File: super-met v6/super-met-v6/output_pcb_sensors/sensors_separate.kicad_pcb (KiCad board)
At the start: 2 copper layers, 99.3 x 99.3 mm, 66 parts, among them J4 Conn_01x08, J5 Conn_01x08, J6 Conn_01x08, J7 Conn_01x04, J8 Conn_01x04, Q13 AO3400A, Q14 AO3400A, Q15 AO3400A, Q16 AO3400A, Q17 AO3400A, Q18 AO3400A, Q19 AO3400A, Q20 AO3400A, Q21 AO3400A, Q22 AO3400A, Q23 AO3400A, Q24 AO3400A, U15 MQ GENERIC BOARD SENSOR, U16 MQ GENERIC BOARD SENSOR, U17 MQ GENERIC BOARD SENSOR, U18 MQ GENERIC BOARD SENSOR, U19 MQ GENERIC BOARD SENSOR, U20 MQ GENERIC BOARD SENSOR, U21 MQ GENERIC BOARD SENSOR, U22 MQ GENERIC BOARD SENSOR, U23 AHT10 MODULE, U24 MQ GENERIC BOARD SENSOR, U25 MQ GENERIC BOARD SENSOR, U26 MICS-6814, U27 CCS811, U28 MS-1100

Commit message: before fill
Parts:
- moved R15 79.3 mm to (67.8, 87.1)
- moved R28 79.3 mm to (83.8, 105.3)
- moved REF**20 79.3 mm to (57.7, 102.4)
- moved REF**22 79.3 mm to (88.3, 75.1)
- moved U23 79.3 mm to (108.0, 107.0)
- moved U27 79.3 mm to (102.7, 90.0)
- moved J4 79.3 mm to (30.8, 33.7)
- moved J5 79.3 mm to (30.8, 65.4)
- moved J6 79.3 mm to (30.8, 96.8)
- moved J7 79.3 mm to (113.6, 91.2)
- moved Q13 79.3 mm to (43.1, 50.9)
- moved Q15 79.3 mm to (84.3, 50.9)
- moved Q16 79.3 mm to (105.2, 51.1)
- moved Q17 79.3 mm to (43.1, 84.8)
- moved Q19 79.3 mm to (84.9, 84.1)
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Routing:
- net Board_0-/Sensors/s1_out: track 28.9 -> 24.9 mm

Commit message: filled
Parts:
- added ?: , , F.Cu at (26.5, 22.3)
- added ?: , , F.Cu at (74.7, 60.9)
- added H2: MountingHole, MountingHole:MountingHole_3.2mm_M3, F.Cu at (108.8, 109.9)
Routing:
- net Board_0-GND2: track 379.3 -> 382.5 mm
- net Board_0-/Sensors/5.2v: track 354.4 -> 353.8 mm
- added copper zone on B.Cu, net (none)
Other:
- board text added: "mq&sensors board"
- board text added: "super-met v0.1"
- board text added: "v&v"

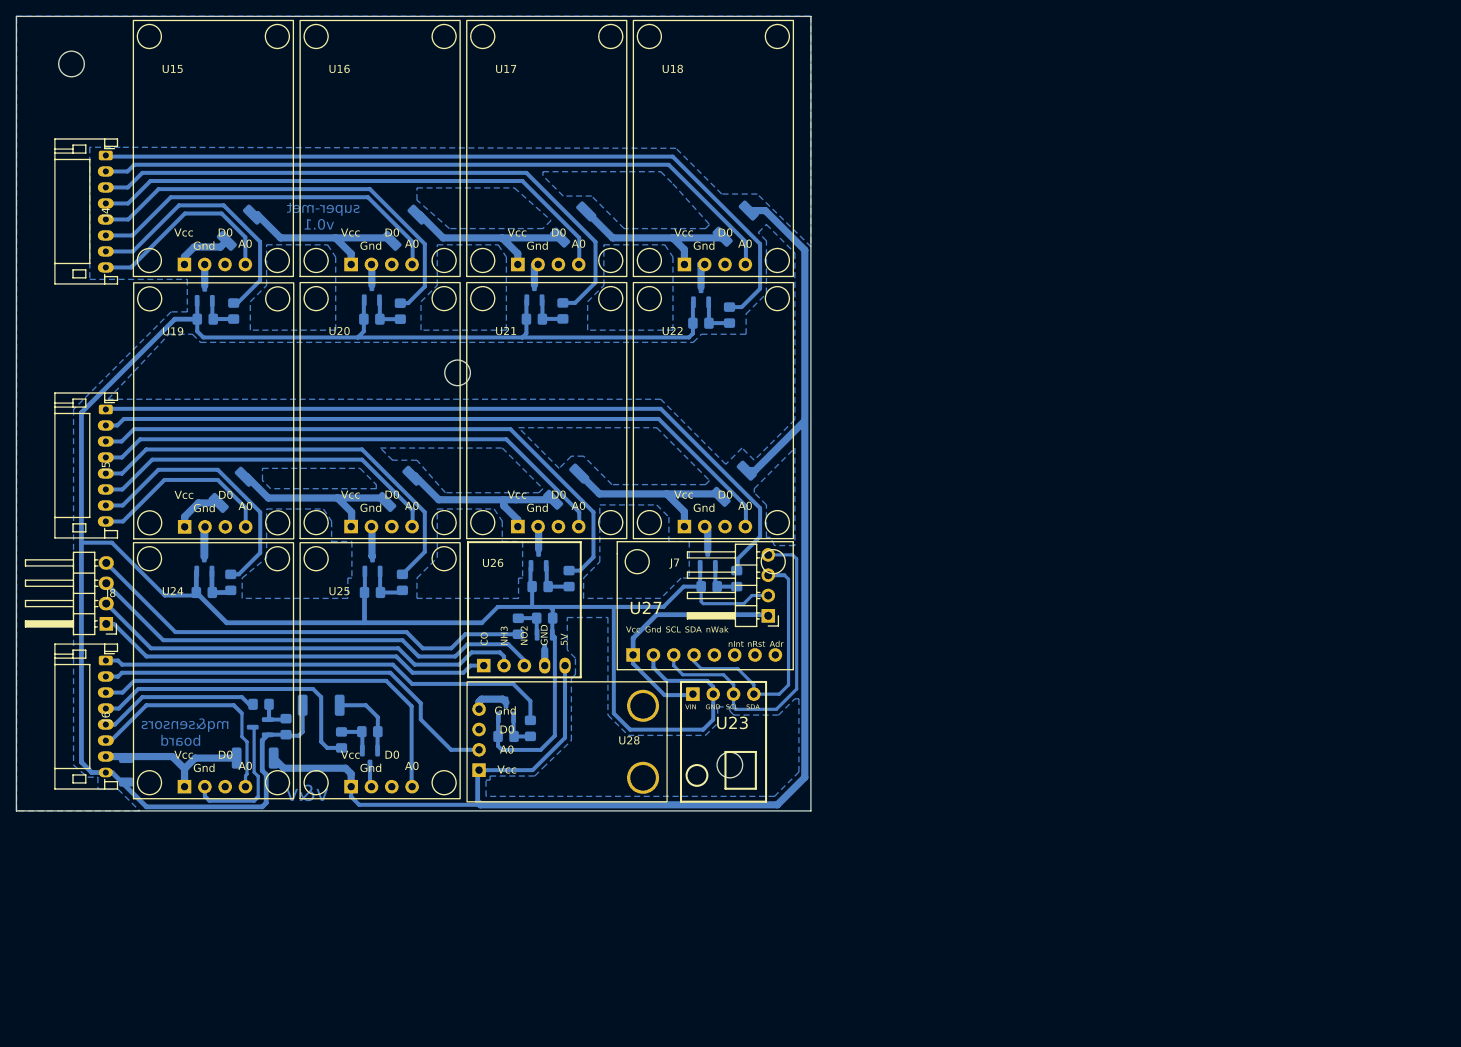
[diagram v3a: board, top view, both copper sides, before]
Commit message: main dc footprint edited
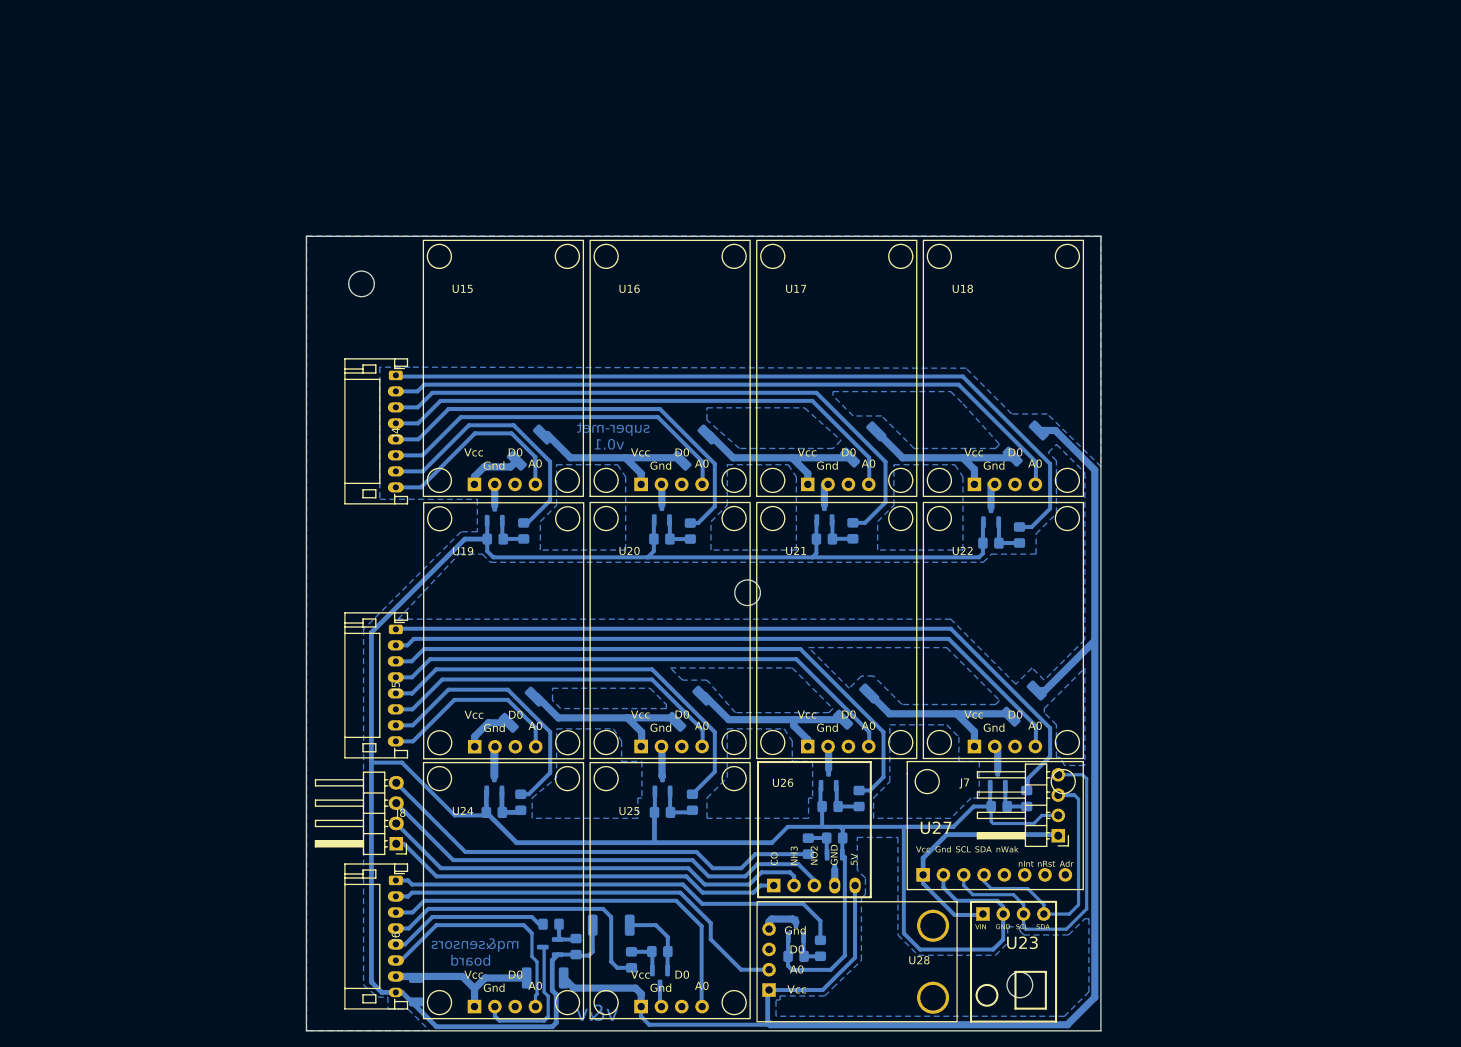
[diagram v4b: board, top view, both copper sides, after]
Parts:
- moved R10 45.5 mm to (79.4, 81.6)
- moved R14 45.5 mm to (82.6, 114.5)
- moved R17 45.5 mm to (145.9, 114.1)
- moved R25 45.5 mm to (100.0, 133.2)
- moved R7 45.5 mm to (103.8, 80.6)
- moved REF**1 45.5 mm to (145.8, 69.7)
- moved REF**20 45.5 mm to (93.9, 129.9)
- moved REF**22 45.5 mm to (124.6, 102.6)
- moved REF**24 45.5 mm to (82.8, 103.0)
- moved U23 45.5 mm to (144.2, 134.5)
- moved ? 45.5 mm to (111.0, 88.4)
- moved C7 45.5 mm to (69.6, 138.0)
- moved H2 45.5 mm to (145.0, 137.4)
- moved J5 45.5 mm to (67.0, 92.9)
- moved J6 45.5 mm to (67.0, 124.3)
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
